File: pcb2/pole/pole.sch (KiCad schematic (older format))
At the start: 21 parts, among them IC1 LMx93, IC2 STM32F0xxKxTx, P1 POWER_IN, P2 BUS_IN, P3 BUS_OUT, P4 SWD_TC, P5 LEDs, Q1 Q_NMOS_GDS, Q2 Q_NMOS_GDS, Q3 Q_NMOS_GDS

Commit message: Removed resistors, added piezo
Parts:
- removed R1, R2, R3, R4, R5, R6: R_Small, agg:0603, symbol R_Small
- added Q?: Q_NMOS_GDS, symbol Q_NMOS_GDS
- added SP?: SPEAKER, symbol SPEAKER
- P1: footprint thegrid:SIL-2 -> thegrid:minipow_edge
- P2, P3: footprint (none) -> agg:S02B-PASK-2
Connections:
- net labels added: PIEZO
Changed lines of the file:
@@
 F 0 "P1" H 3050 3000 50  0000 C CNN
 F 1 "POWER_IN" V 3150 2850 50  0000 C CNN
-F 2 "thegrid:SIL-2" H 3050 2850 50  0001 C CNN
+F 2 "thegrid:minipow_edge" H 3050 2850 50  0001 C CNN
 F 3 "" H 3050 2850 50  0000 C CNN
 	1    3050 2850
@@
 F 0 "P2" H 3050 3700 50  0000 C CNN
 F 1 "BUS_IN" V 3150 3500 50  0000 C CNN
-F 2 "" H 3050 3550 50  0000 C CNN
+F 2 "agg:S02B-PASK-2" H 3050 3550 50  0001 C CNN
 F 3 "" H 3050 3550 50  0000 C CNN
 	1    3050 3550
@@
 F 0 "P3" H 3050 4000 50  0000 C CNN
 F 1 "BUS_OUT" V 3150 3900 50  0000 C CNN
-F 2 "" H 3050 3850 50  0000 C CNN
+F 2 "agg:S02B-PASK-2" H 3050 3850 50  0001 C CNN
 F 3 "" H 3050 3850 50  0000 C CNN
 	1    3050 3850
@@
 	1    0    0    -1
 $EndComp
-$Comp
-L R_Small R1
-U 1 1 56F1E254
-P 7500 3450
-F 0 "R1" H 7530 3470 50  0000 L CNN
-F 1 "R_Small" H 7530 3410 50  0000 L CNN
-F 2 "agg:0603" H 7500 3450 50  0001 C CNN
-F 3 "" H 7500 3450 50  0000 C CNN
-	1    7500 3450
-	0    -1   -1   0
-$EndComp
-$Comp
-L R_Small R4
-U 1 1 56F1E299
-P 7600 3550
-F 0 "R4" H 7630 3570 50  0000 L CNN
-F 1 "R_Small" H 7630 3510 50  0000 L CNN
-F 2 "agg:0603" H 7600 3550 50  0001 C CNN
-F 3 "" H 7600 3550 50  0000 C CNN
-	1    7600 3550
-	1    0    0    -1
-$EndComp
-Connection ~ 7600 3450
-$Comp
-L GND #PWR019
-U 1 1 56F1E348
-P 7600 3650
-F 0 "#PWR019" H 7600 3400 50  0001 C CNN
-F 1 "GND" H 7600 3500 50  0000 C CNN
-F 2 "" H 7600 3650 50  0000 C CNN
-F 3 "" H 7600 3650 50  0000 C CNN
-	1    7600 3650
-	1    0    0    -1
-$EndComp
-Text Label 7400 3450 2    60   ~ 0
+Text Label 7600 3450 2    60   ~ 0
 LED_R
 $Comp
@@
 	1    0    0    -1
 $EndComp
-$Comp
-L R_Small R2
-U 1 1 56F1E528
-P 7500 4200
-F 0 "R2" H 7530 4220 50  0000 L CNN
-F 1 "R_Small" H 7530 4160 50  0000 L CNN
-F 2 "agg:0603" H 7500 4200 50  0001 C CNN
-F 3 "" H 7500 4200 50  0000 C CNN
-	1    7500 4200
-	0    -1   -1   0
-$EndComp
-$Comp
-L R_Small R5
-U 1 1 56F1E52E
-P 7600 4300
-F 0 "R5" H 7630 4320 50  0000 L CNN
-F 1 "R_Small" H 7630 4260 50  0000 L CNN
-F 2 "agg:0603" H 7600 4300 50  0001 C CNN
-F 3 "" H 7600 4300 50  0000 C CNN
-	1    7600 4300
-	1    0    0    -1
-$EndComp
-Connection ~ 7600 4200
-$Comp
-L GND #PWR021
-U 1 1 56F1E535
-P 7600 4400
-F 0 "#PWR021" H 7600 4150 50  0001 C CNN
-F 1 "GND" H 7600 4250 50  0000 C CNN
-F 2 "" H 7600 4400 50  0000 C CNN
-F 3 "" H 7600 4400 50  0000 C CNN
-	1    7600 4400
-	1    0    0    -1
-$EndComp
-Text Label 7400 4200 2    60   ~ 0
+Text Label 7600 4200 2    60   ~ 0
 LED_G
 $Comp
@@
 	1    0    0    -1
 $EndComp
-$Comp
-L R_Small R3
-U 1 1 56F1E677
-P 7500 4950
-F 0 "R3" H 7530 4970 50  0000 L CNN
-F 1 "R_Small" H 7530 4910 50  0000 L CNN
-F 2 "agg:0603" H 7500 4950 50  0001 C CNN
-F 3 "" H 7500 4950 50  0000 C CNN
-	1    7500 4950
-	0    -1   -1   0
-$EndComp
-$Comp
-L R_Small R6
-U 1 1 56F1E67D
-P 7600 5050
-F 0 "R6" H 7630 5070 50  0000 L CNN
-F 1 "R_Small" H 7630 5010 50  0000 L CNN
-F 2 "agg:0603" H 7600 5050 50  0001 C CNN
-F 3 "" H 7600 5050 50  0000 C CNN
-	1    7600 5050
-	1    0    0    -1
-$EndComp
-Connection ~ 7600 4950
-$Comp
-L GND #PWR023
-U 1 1 56F1E684
-P 7600 5150
-F 0 "#PWR023" H 7600 4900 50  0001 C CNN
-F 1 "GND" H 7600 5000 50  0000 C CNN
-F 2 "" H 7600 5150 50  0000 C CNN
-F 3 "" H 7600 5150 50  0000 C CNN
-	1    7600 5150
-	1    0    0    -1
-$EndComp
-Text Label 7400 4950 2    60   ~ 0
+Text Label 7600 4950 2    60   ~ 0
 LED_B
 Text Label 6150 3050 0    60   ~ 0
@@
 	1    0    0    -1
 $EndComp
+Text Label 6150 3450 0    60   ~ 0
+PIEZO
+Text Label 9250 5600 2    60   ~ 0
+PIEZO
+$Comp
+L Q_NMOS_GDS Q?
+U 1 1 56F591D2
+P 9450 5600
+F 0 "Q?" H 9750 5650 50  0000 R CNN
+F 1 "Q_NMOS_GDS" H 10100 5550 50  0000 R CNN
+F 2 "" H 9650 5700 50  0000 C CNN
+F 3 "" H 9450 5600 50  0000 C CNN
+	1    9450 5600
+	1    0    0    -1
+$EndComp
+$Comp
+L GND #PWR?
+U 1 1 56F594BA
+P 9550 5800
+F 0 "#PWR?" H 9550 5550 50  0001 C CNN
+F 1 "GND" H 9550 5650 50  0000 C CNN
+F 2 "" H 9550 5800 50  0000 C CNN
+F 3 "" H 9550 5800 50  0000 C CNN
+	1    9550 5800
+	1    0    0    -1
+$EndComp
+$Comp
+L SPEAKER SP?
+U 1 1 56F594FE
+P 9850 5300
+F 0 "SP?" H 9750 5550 50  0000 C CNN
+F 1 "SPEAKER" H 9750 5650 50  0000 C CNN
+F 2 "" H 9850 5300 50  0000 C CNN
+F 3 "" H 9850 5300 50  0000 C CNN
+	1    9850 5300
+	1    0    0    -1
+$EndComp
+$Comp
+L +12V #PWR?
+U 1 1 56F59754
+P 9550 5200
+F 0 "#PWR?" H 9550 5050 50  0001 C CNN
+F 1 "+12V" H 9550 5340 50  0000 C CNN
+F 2 "" H 9550 5200 50  0000 C CNN
+F 3 "" H 9550 5200 50  0000 C CNN
+	1    9550 5200
+	1    0    0    -1
+$EndComp

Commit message: Added piezo fp
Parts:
- SP?: footprint (none) -> thegrid:piezo
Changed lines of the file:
@@
 F 0 "SP?" H 9750 5550 50  0000 C CNN
 F 1 "SPEAKER" H 9750 5650 50  0000 C CNN
-F 2 "" H 9850 5300 50  0000 C CNN
-F 3 "" H 9850 5300 50  0000 C CNN
+F 2 "thegrid:piezo" H 9850 5300 50  0001 C CNN
+F 3 "1823866" H 9850 5300 50  0001 C CNN
 	1    9850 5300
 	1    0    0    -1

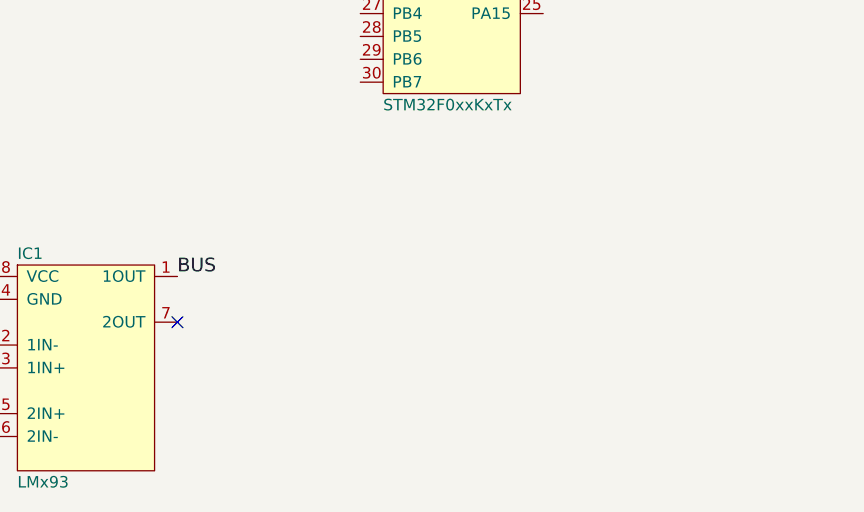
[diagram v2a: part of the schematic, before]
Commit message: VREG footprint
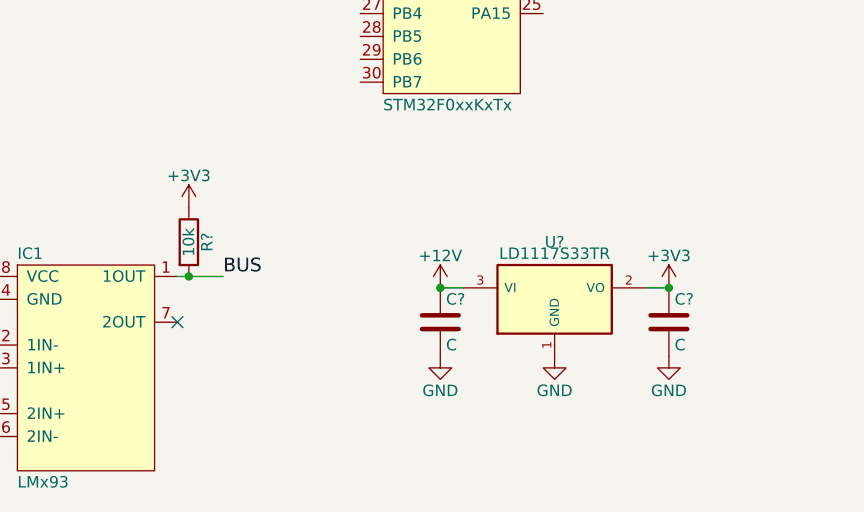
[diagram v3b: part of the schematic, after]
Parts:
- added C? (x2): C, agg:0603, symbol C
- added R?: 10k, agg:0603, symbol R
- added U?: LD1117S33TR, thegrid:TO-252-3, symbol LD1117S33TR
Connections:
- net +12V: now also C?.1, U?.3 (VI)
- net +3V3: now also C?.1, R?.1, U?.2 (VO)
- net BUS: now also R?.2
- net GND: now also C?.2, C?.2, U?.1 (GND)
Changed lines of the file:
@@
 	3250 5900 3150 5900
 Connection ~ 3150 6000
-Text Label 4050 5300 0    60   ~ 0
+Text Label 4250 5300 0    60   ~ 0
 BUS
 $Comp
@@
 	1    0    0    -1
 $EndComp
+$Comp
+L R R?
+U 1 1 56F5991E
+P 4100 5150
+F 0 "R?" V 4180 5150 50  0000 C CNN
+F 1 "10k" V 4100 5150 50  0000 C CNN
+F 2 "agg:0603" V 4030 5150 50  0001 C CNN
+F 3 "" H 4100 5150 50  0000 C CNN
+	1    4100 5150
+	1    0    0    -1
+$EndComp
+Wire Wire Line
+	4050 5300 4250 5300
+Connection ~ 4100 5300
+$Comp
+L +3V3 #PWR?
+U 1 1 56F59A49
+P 4100 5000
+F 0 "#PWR?" H 4100 4850 50  0001 C CNN
+F 1 "+3V3" H 4100 5140 50  0000 C CNN
+F 2 "" H 4100 5000 50  0000 C CNN
+F 3 "" H 4100 5000 50  0000 C CNN
+	1    4100 5000
+	1    0    0    -1
+$EndComp
+$Comp
+L LD1117S33TR U?
+U 1 1 56F59E11
+P 5700 5400
+F 0 "U?" H 5700 5650 50  0000 C CNN
+F 1 "LD1117S33TR" H 5700 5600 50  0000 C CNN
+F 2 "thegrid:TO-252-3" H 5700 5500 50  0001 C CNN
+F 3 "http://www.farnell.com/datasheets/93498.pdf" H 5700 5400 50  0001 C CNN
+	1    5700 5400
+	1    0    0    -1
+$EndComp
+$Comp
+L +12V #PWR?
+U 1 1 56F59EBA
+P 5200 5350
+F 0 "#PWR?" H 5200 5200 50  0001 C CNN
+F 1 "+12V" H 5200 5490 50  0000 C CNN
+F 2 "" H 5200 5350 50  0000 C CNN
+F 3 "" H 5200 5350 50  0000 C CNN
+	1    5200 5350
+	1    0    0    -1
+$EndComp
+$Comp
+L C C?
+U 1 1 56F59EF4
+P 5200 5500
+F 0 "C?" H 5225 5600 50  0000 L CNN
+F 1 "C" H 5225 5400 50  0000 L CNN
+F 2 "agg:0603" H 5238 5350 50  0001 C CNN
+F 3 "" H 5200 5500 50  0000 C CNN
+	1    5200 5500
+	1    0    0    -1
+$EndComp
+$Comp
+L GND #PWR?
+U 1 1 56F59F39
+P 5200 5650
+F 0 "#PWR?" H 5200 5400 50  0001 C CNN
+F 1 "GND" H 5200 5500 50  0000 C CNN
+F 2 "" H 5200 5650 50  0000 C CNN
+F 3 "" H 5200 5650 50  0000 C CNN
+	1    5200 5650
+	1    0    0    -1
+$EndComp
+Connection ~ 5200 5350
+Wire Wire Line
+	5200 5350 5300 5350
+$Comp
+L +3V3 #PWR?
+U 1 1 56F59FB2
+P 6200 5350
+F 0 "#PWR?" H 6200 5200 50  0001 C CNN
+F 1 "+3V3" H 6200 5490 50  0000 C CNN
+F 2 "" H 6200 5350 50  0000 C CNN
+F 3 "" H 6200 5350 50  0000 C CNN
+	1    6200 5350
+	1    0    0    -1
+$EndComp
+Connection ~ 6200 5350
+Wire Wire Line
+	6200 5350 6100 5350
+$Comp
+L C C?
+U 1 1 56F5A02D
+P 6200 5500
+F 0 "C?" H 6225 5600 50  0000 L CNN
+F 1 "C" H 6225 5400 50  0000 L CNN
+F 2 "agg:0603" H 6238 5350 50  0001 C CNN
+F 3 "" H 6200 5500 50  0000 C CNN
+	1    6200 5500
+	1    0    0    -1
+$EndComp
+$Comp
+L GND #PWR?
+U 1 1 56F5A070
+P 6200 5650
+F 0 "#PWR?" H 6200 5400 50  0001 C CNN
+F 1 "GND" H 6200 5500 50  0000 C CNN
+F 2 "" H 6200 5650 50  0000 C CNN
+F 3 "" H 6200 5650 50  0000 C CNN
+	1    6200 5650
+	1    0    0    -1
+$EndComp
+$Comp
+L GND #PWR?
+U 1 1 56F5A0AE
+P 5700 5650
+F 0 "#PWR?" H 5700 5400 50  0001 C CNN
+F 1 "GND" H 5700 5500 50  0000 C CNN
+F 2 "" H 5700 5650 50  0000 C CNN
+F 3 "" H 5700 5650 50  0000 C CNN
+	1    5700 5650
+	1    0    0    -1
+$EndComp

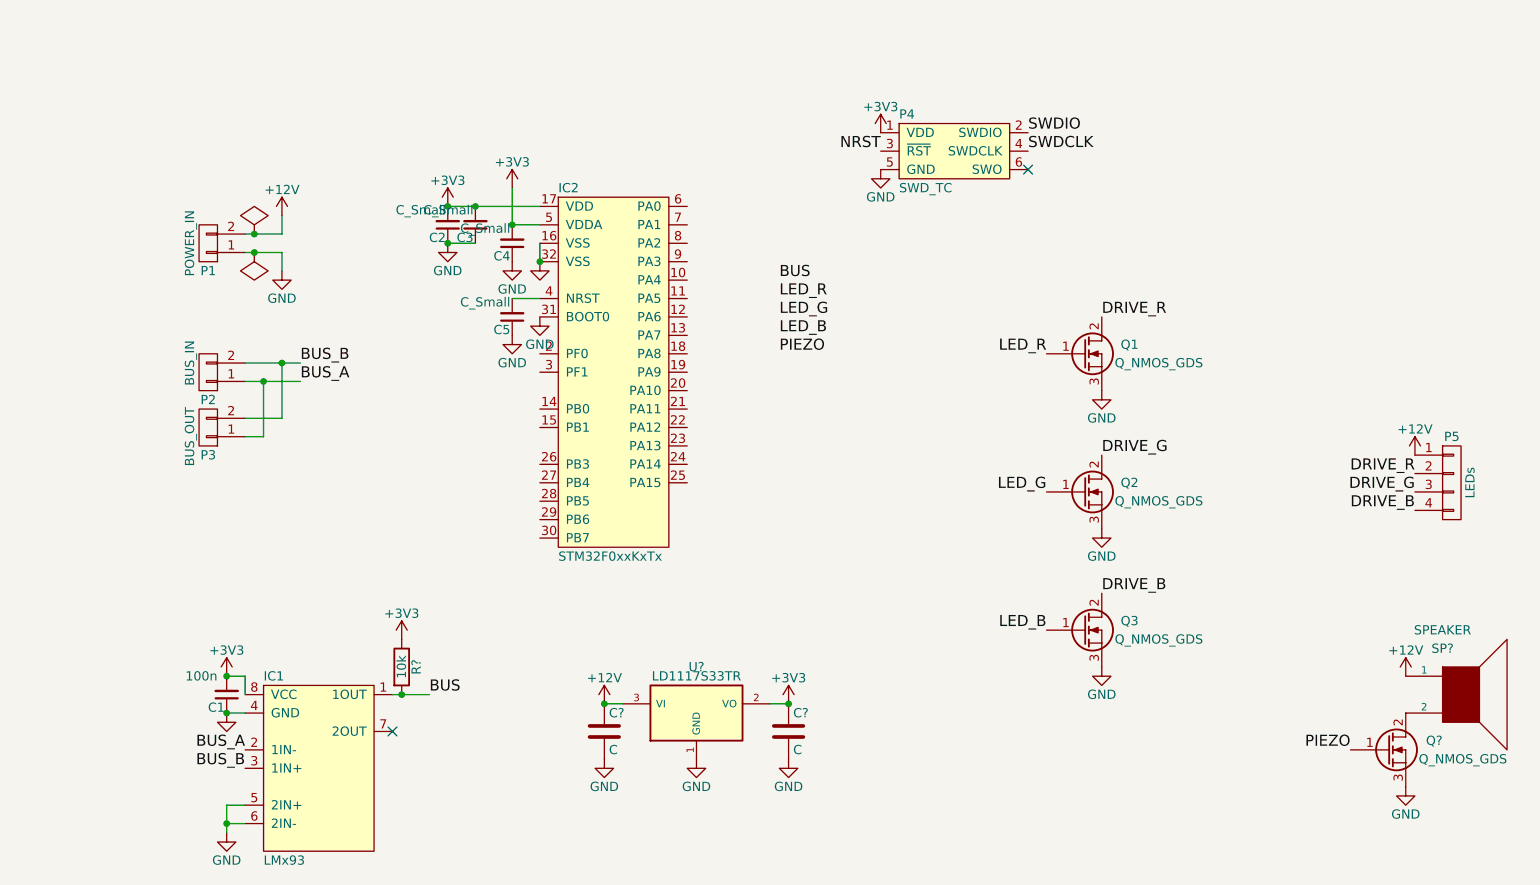
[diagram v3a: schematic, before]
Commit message: Chose NMOS, added fp etc
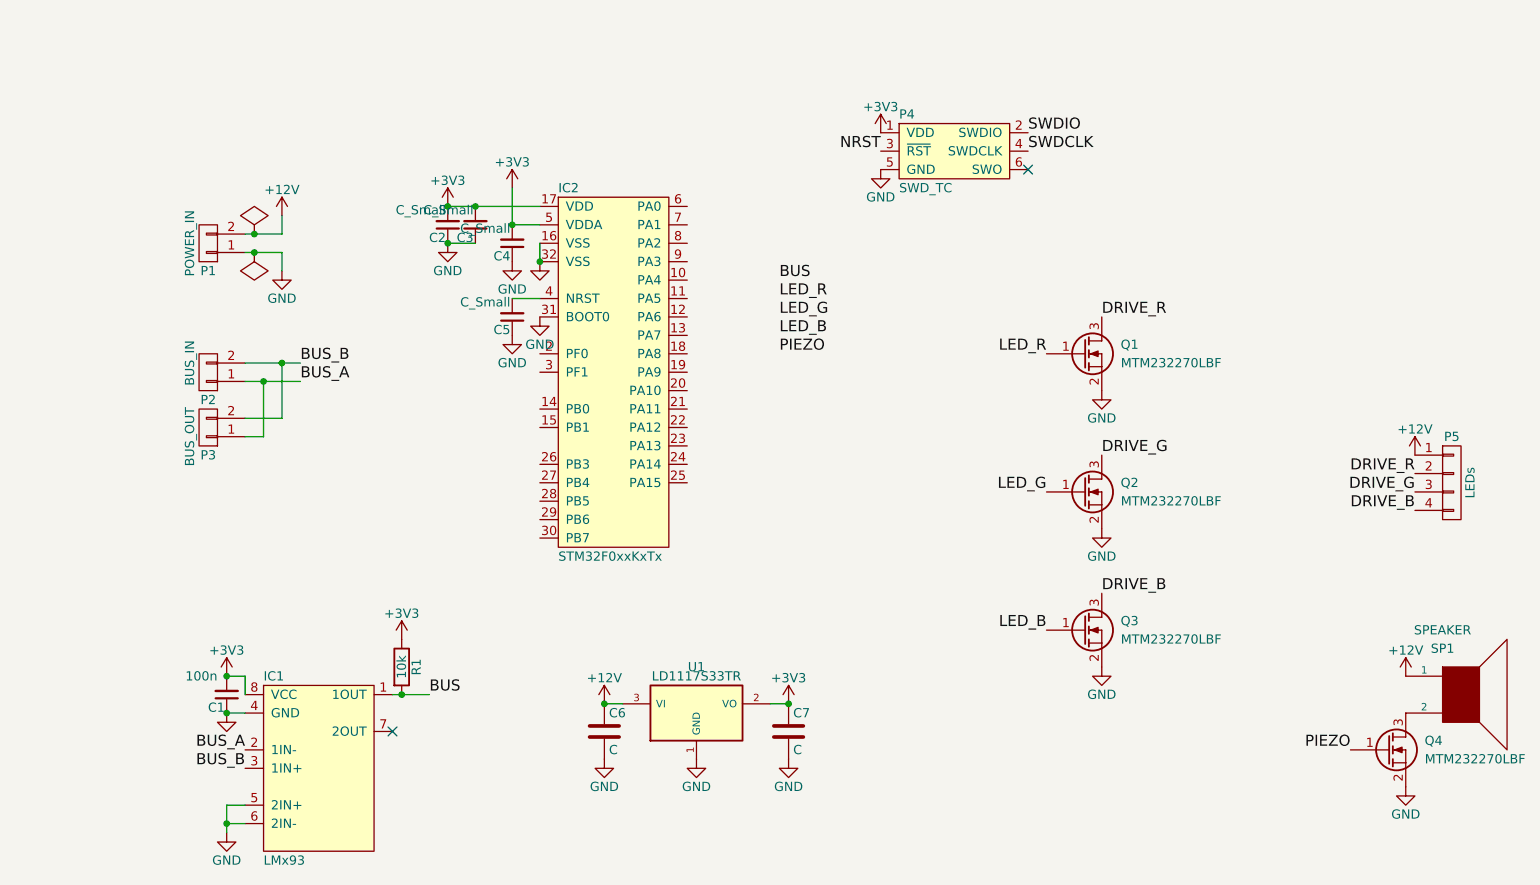
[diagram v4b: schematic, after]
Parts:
- removed Q1, Q2, Q3, Q?: Q_NMOS_GDS, symbol Q_NMOS_GDS
- added Q1, Q2, Q3, Q4: MTM232270LBF, thegrid:SOT-323, symbol Q_NMOS_GSD
- gave numbers to parts that had none: 5
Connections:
- net DRIVE_B: now also Q3.3 (D)
- net DRIVE_G: now also Q2.3 (D)
- net DRIVE_R: now also Q1.3 (D)
- net GND: now also Q1.2 (S), Q2.2 (S), Q3.2 (S), Q4.2 (S)
- net LED_B: now also Q3.1 (G)
- net LED_G: now also Q2.1 (G)
- net LED_R: now also Q1.1 (G)
- net PIEZO: now also Q4.1 (G)
- net at SP1.2: now also Q4.3 (D)

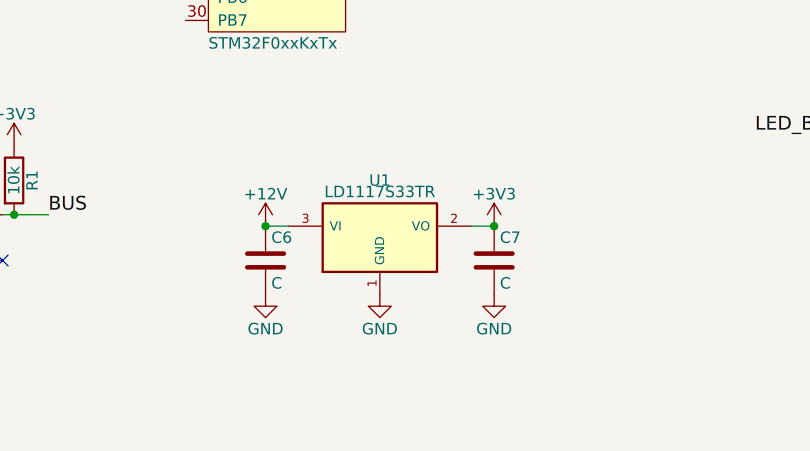
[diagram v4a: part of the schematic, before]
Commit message: VREG capacitor values
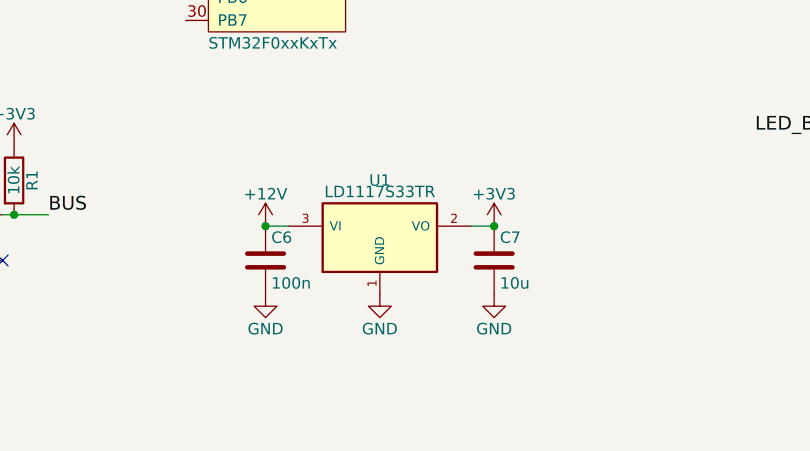
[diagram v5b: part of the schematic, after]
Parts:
- C6: value C -> 100n
- C7: value C -> 10u
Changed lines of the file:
@@
 P 5200 5500
 F 0 "C6" H 5225 5600 50  0000 L CNN
-F 1 "C" H 5225 5400 50  0000 L CNN
+F 1 "100n" H 5225 5400 50  0000 L CNN
 F 2 "agg:0603" H 5238 5350 50  0001 C CNN
 F 3 "" H 5200 5500 50  0000 C CNN
@@
 P 6200 5500
 F 0 "C7" H 6225 5600 50  0000 L CNN
-F 1 "C" H 6225 5400 50  0000 L CNN
+F 1 "10u" H 6225 5400 50  0000 L CNN
 F 2 "agg:0603" H 6238 5350 50  0001 C CNN
 F 3 "" H 6200 5500 50  0000 C CNN
